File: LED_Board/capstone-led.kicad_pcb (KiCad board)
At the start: 4 copper layers, 127 x 127 mm, 296 parts

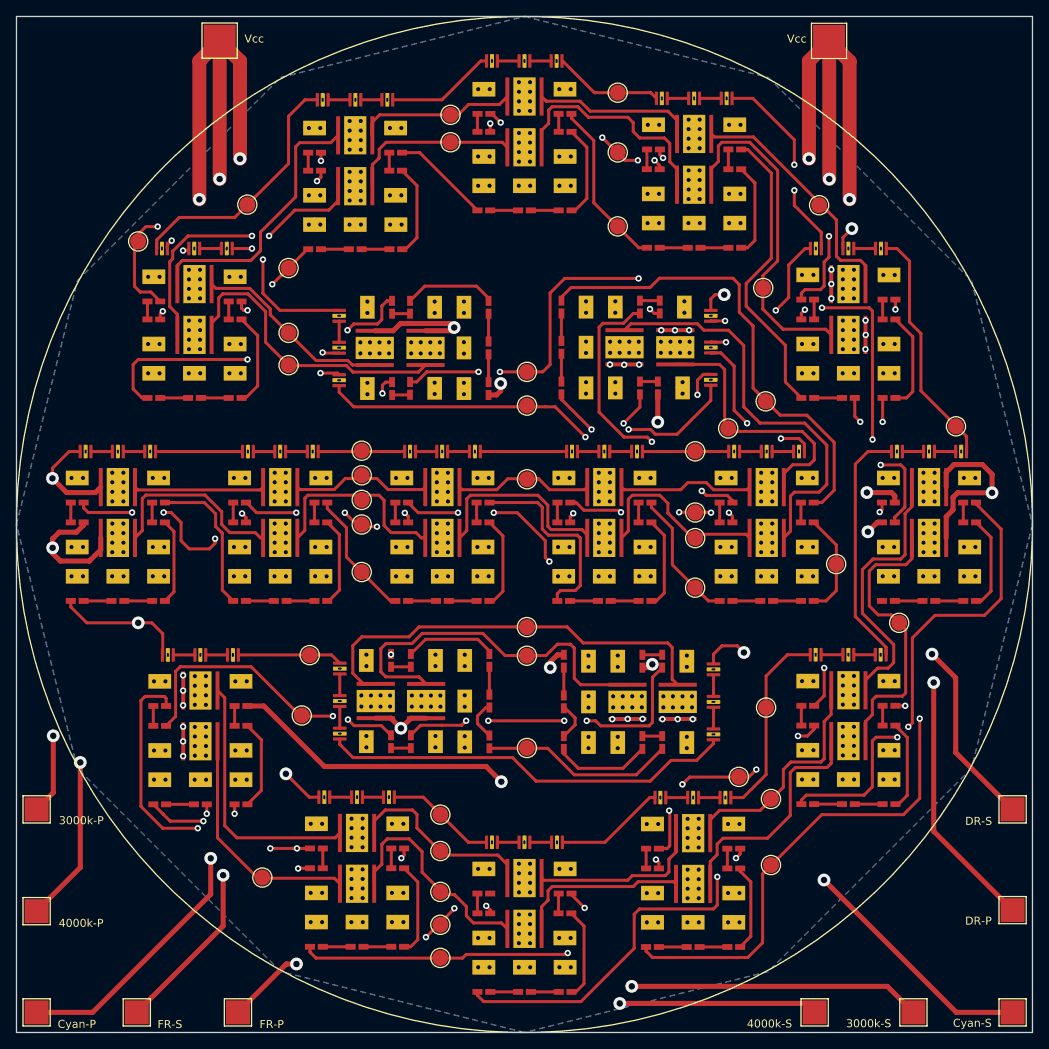
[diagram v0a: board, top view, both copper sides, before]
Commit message: Drill Holes, Vcc Fill Zones, Thicker Vcc Traces
Finalizing design for review before sending to manufacturing
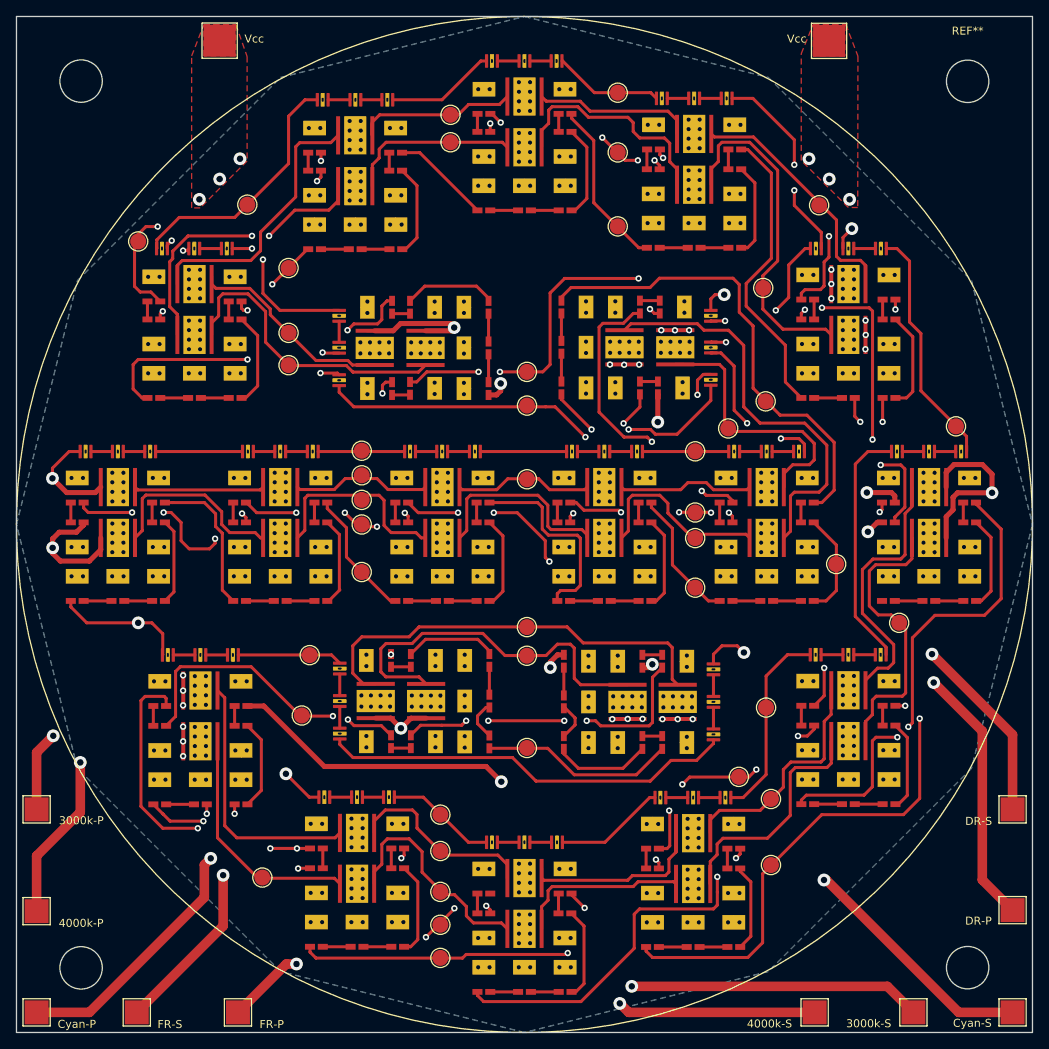
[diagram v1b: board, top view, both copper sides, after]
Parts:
- added REF**: MountingHole_5.3mm_M5, MountingHole:MountingHole_5.3mm_M5, F.Cu at (43.6, 43.6)
- added REF**: MountingHole_5.3mm_M5, MountingHole:MountingHole_5.3mm_M5, F.Cu at (154.5, 43.7)
- added REF**: MountingHole_5.3mm_M5, MountingHole:MountingHole_5.3mm_M5, F.Cu at (154.5, 154.5)
- added REF**: MountingHole_5.3mm_M5, MountingHole:MountingHole_5.3mm_M5, F.Cu at (43.6, 154.5)
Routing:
- net VCC: track 209.6 -> 101.7 mm
- added copper zone on F.Cu, net VCC
